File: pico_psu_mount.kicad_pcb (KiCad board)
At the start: 2 copper layers, 54.9 x 30.7 mm, 3 parts, among them J1 Conn_01x02, U1 DreamcastPower, U2 atx_24pin

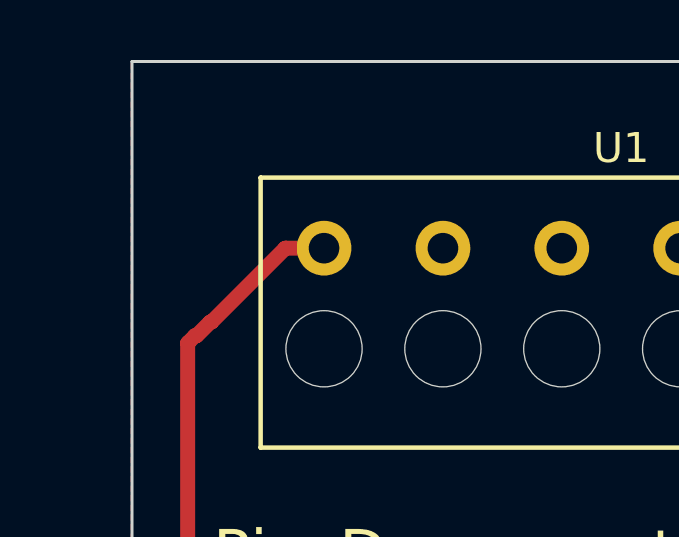
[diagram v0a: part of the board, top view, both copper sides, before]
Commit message: fixed: PicoPSU does not turns off properly, when no load is present on the 12V rail
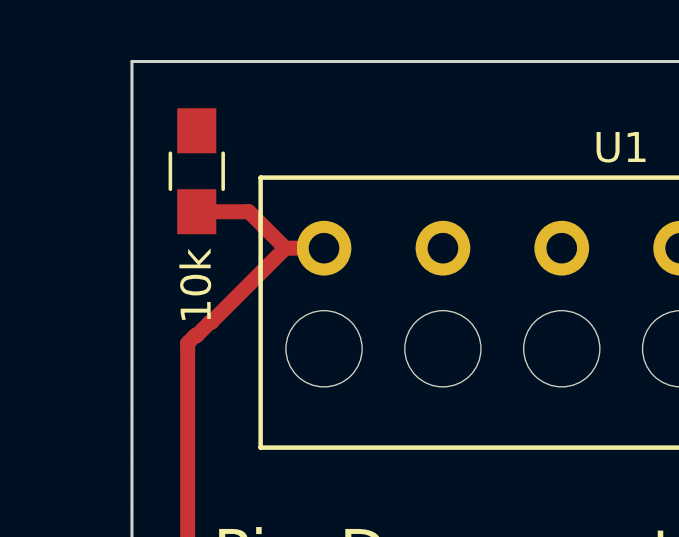
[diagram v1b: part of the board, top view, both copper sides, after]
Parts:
- added 10k: R, Resistors_SMD:R_0805_HandSoldering, F.Cu at (149.5, 68.0)
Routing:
- net /12V: track 32.1 -> 35.6 mm
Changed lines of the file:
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@@
-(kicad_pcb (version 20171130) (host pcbnew "(5.0.0)")
+(kicad_pcb (version 20171130) (host pcbnew "(5.0.0-3-g5ebb6b6)")
   (general
     (thickness 1.6)
     (drawings 6)
-    (tracks 31)
+    (tracks 33)
     (zones 0)
-    (modules 3)
+    (modules 4)
     (nets 18)
   )
@@
     (pad "" np_thru_hole circle (at 11.8872 -6.7056 180) (size 2.54 2.54) (drill 2.54) (layers *.Cu *.Mask))
   )
+  (module Resistors_SMD:R_0805_HandSoldering (layer F.Cu)
+    (at 149.4536 67.9704 90)
+    (descr "Resistor SMD 0805, hand soldering")
+    (tags "resistor 0805")
+    (attr smd)
+    (fp_text reference 10k (at -3.8354 0 90) (layer F.SilkS)
+      (effects (font (size 1 1) (thickness 0.15)))
+    )
+    (fp_text value R (at 1.5748 1.5748 180) (layer F.Fab)
+      (effects (font (size 1 1) (thickness 0.15)))
+    )
+    (fp_line (start 2.35 0.9) (end -2.35 0.9) (layer F.CrtYd) (width 0.05))
+    (fp_line (start 2.35 0.9) (end 2.35 -0.9) (layer F.CrtYd) (width 0.05))
+    (fp_line (start -2.35 -0.9) (end -2.35 0.9) (layer F.CrtYd) (width 0.05))
+    (fp_line (start -2.35 -0.9) (end 2.35 -0.9) (layer F.CrtYd) (width 0.05))
+    (fp_line (start -0.6 -0.88) (end 0.6 -0.88) (layer F.SilkS) (width 0.12))
+    (fp_line (start 0.6 0.88) (end -0.6 0.88) (layer F.SilkS) (width 0.12))
+    (fp_line (start -1 -0.62) (end 1 -0.62) (layer F.Fab) (width 0.1))
+    (fp_line (start 1 -0.62) (end 1 0.62) (layer F.Fab) (width 0.1))
+    (fp_line (start 1 0.62) (end -1 0.62) (layer F.Fab) (width 0.1))
+    (fp_line (start -1 0.62) (end -1 -0.62) (layer F.Fab) (width 0.1))
+    (fp_text user %R (at 2.8194 0 180) (layer F.Fab)
+      (effects (font (size 0.5 0.5) (thickness 0.075)))
+    )
+    (pad 2 smd rect (at 1.35 0 90) (size 1.5 1.3) (layers F.Cu F.Paste F.Mask)
+      (net 1 GND))
+    (pad 1 smd rect (at -1.35 0 90) (size 1.5 1.3) (layers F.Cu F.Paste F.Mask)
+      (net 15 /12V))
+    (model ${KISYS3DMOD}/Resistors_SMD.3dshapes/R_0805.wrl
+      (at (xyz 0 0 0))
+      (scale (xyz 1 1 1))
+      (rotate (xyz 0 0 0))
+    )
+  )
   (gr_text "PicoDreamcast v1.1" (at 150 80.7) (layer F.SilkS)
     (effects (font (size 1.5 1.5) (thickness 0.3)) (justify left))
@@
   (segment (start 149.15 87.2) (end 150.45 88.5) (width 0.5) (layer F.Cu) (net 15))
   (segment (start 149.15 73.7) (end 149.15 87.2) (width 0.5) (layer F.Cu) (net 15))
+  (segment (start 151.190238 69.3204) (end 152.405638 70.5358) (width 0.5) (layer F.Cu) (net 15))
+  (segment (start 149.4536 69.3204) (end 151.190238 69.3204) (width 0.5) (layer F.Cu) (net 15))
   (zone (net 1) (net_name GND) (layer B.Cu) (hatch edge 0.508)
     (connect_pads (clearance 0.508))
